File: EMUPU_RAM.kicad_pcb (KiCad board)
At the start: 2 copper layers, 99.1 x 82.5 mm, 29 parts, among them J1 Conn_01x20_Socket, J2 Conn_01x20_Socket, J3 Barrel_Jack_Switch, J4 Conn_01x06_Pin, J5 Conn_01x08_Pin, J6 Conn_01x06_Pin, J7 Conn_01x02_Pin, SW1 SW_SPDT, SW2 SW_SPST, U1 PIC18F57Q43-IPT, U2 HM678127_SOJ32_Arranged

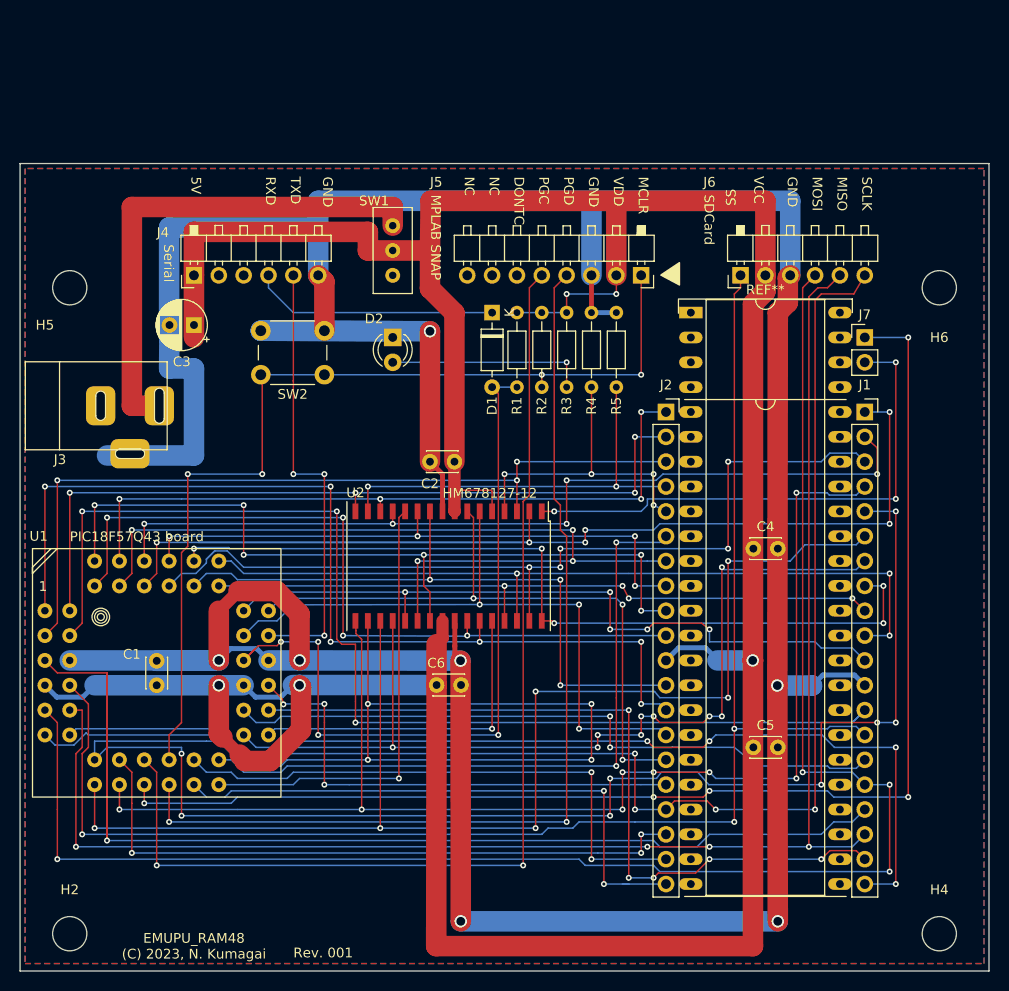
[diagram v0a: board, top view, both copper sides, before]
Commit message: Add Z80 label, RBx jumpers, garbers, ZIP
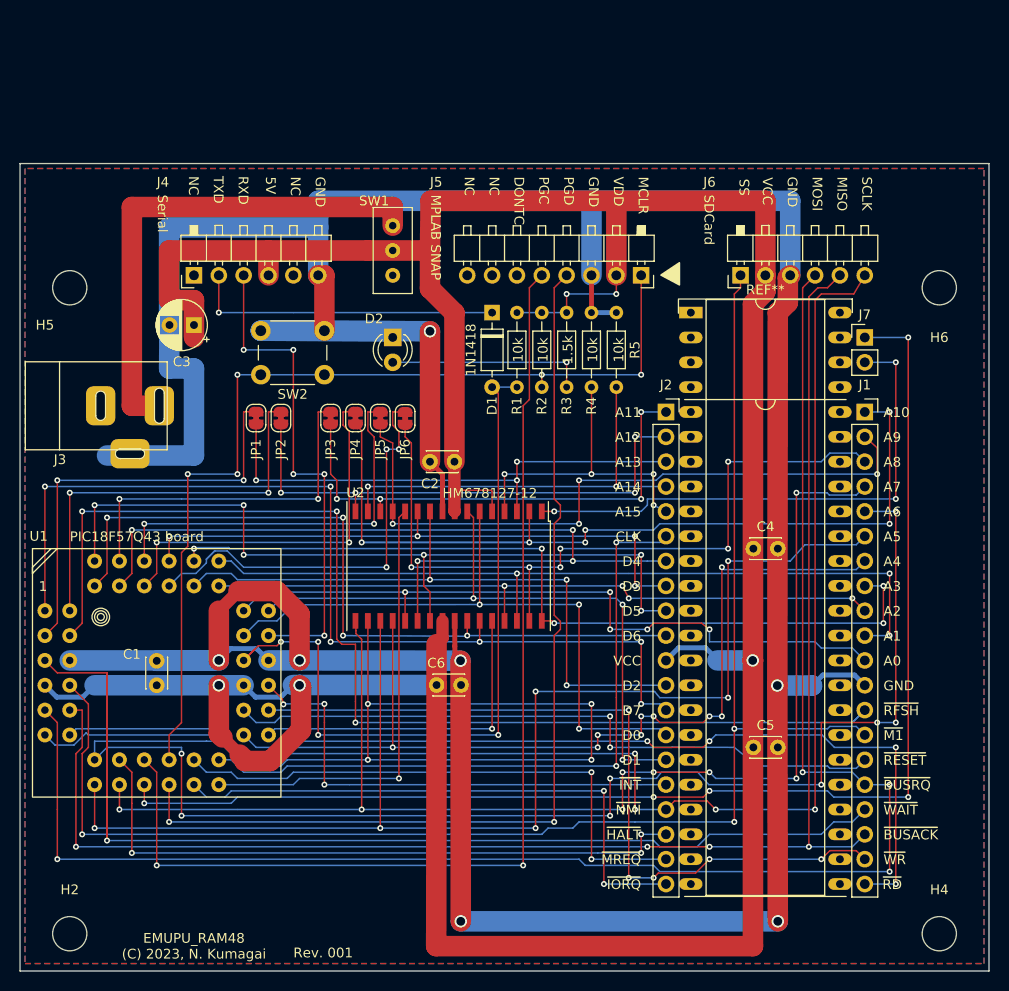
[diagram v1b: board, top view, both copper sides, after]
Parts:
- added JP1: SolderJumper_2_Bridged, Jumper:SolderJumper-2_P1.3mm_Bridged_RoundedPad1.0x1.5mm, F.Cu at (108.0, 84.4)
- added JP2: SolderJumper_2_Bridged, Jumper:SolderJumper-2_P1.3mm_Bridged_RoundedPad1.0x1.5mm, F.Cu at (110.5, 84.4)
- added JP3: SolderJumper_2_Bridged, Jumper:SolderJumper-2_P1.3mm_Bridged_RoundedPad1.0x1.5mm, F.Cu at (115.6, 84.4)
- added JP4: SolderJumper_2_Bridged, Jumper:SolderJumper-2_P1.3mm_Bridged_RoundedPad1.0x1.5mm, F.Cu at (118.1, 84.4)
- added JP5: SolderJumper_2_Bridged, Jumper:SolderJumper-2_P1.3mm_Bridged_RoundedPad1.0x1.5mm, F.Cu at (120.7, 84.4)
- added JP6: SolderJumper_2_Bridged, Jumper:SolderJumper-2_P1.3mm_Bridged_RoundedPad1.0x1.5mm, F.Cu at (123.2, 84.5)
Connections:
- J4 pad 1: VCC -> unconnected-(J4-Pin_1-Pad1)
- J4 pad 2: unconnected-(J4-Pin_2-Pad2) -> Net-(D1-K)
- J4 pad 3: unconnected-(J4-Pin_3-Pad3) -> Net-(J4-Pin_3)
- J4 pad 4: Net-(D1-K) -> VCC
- J4 pad 5: Net-(J4-Pin_5) -> unconnected-(J4-Pin_5-Pad5)
- U1 pad 2: /A12 -> Net-(JP2-B)
- U1 pad 3: /A13 -> Net-(JP1-B)
- U1 pad 33: Net-(J4-Pin_5) -> Net-(J4-Pin_3)
- U1 pad 42: /A8 -> Net-(JP6-B)
- U1 pad 43: /A9 -> Net-(JP5-B)
- U1 pad 44: /A10 -> Net-(JP4-B)
- U1 pad 45: /A11 -> Net-(JP3-B)
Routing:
- net Net-(J4-Pin_3): track 0.00 -> 50.8 mm, vias 0 -> 5
- net Net-(J4-Pin_5): track 45.7 -> 0.00 mm, vias 3 -> 0
- net Net-(JP6-B): track 0.00 -> 44.5 mm, vias 0 -> 3
- net Net-(JP1-B): track 0.00 -> 43.7 mm, vias 0 -> 2
- net Net-(JP2-B): track 0.00 -> 41.9 mm, vias 0 -> 2
- net Net-(JP5-B): track 0.00 -> 40.3 mm, vias 0 -> 2
- net Net-(JP4-B): track 0.00 -> 39.5 mm, vias 0 -> 2
- net Net-(JP3-B): track 0.00 -> 36.8 mm, vias 0 -> 2
- net /A13: track 83.7 -> 52.7 mm
- net /A10: track 132.4 -> 102.1 mm
- net /A12: track 80.6 -> 54.0 mm
- net /A11: track 72.4 -> 51.7 mm
- net /A9: track 89.1 -> 69.5 mm, vias 5 -> 4
- net /A8: track 91.7 -> 78.2 mm, vias 5 -> 6
- net Net-(D1-K): track 25.2 -> 31.8 mm, vias 0 -> 1
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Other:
- board text added: "1.5k"
- board text added: "10k"
- board text added: "A0"
- board text added: "A1"
- board text added: "A10"
- board text added: "A11"
- board text added: "A12"
- board text added: "A13"
- board text added: "A14"
- board text added: "A15"
- board text added: "A2"
- board text added: "A3"
- board text added: "A4"
- board text added: "A5"
- board text added: "A6"
- board text added: "A7"
- board text added: "A8"
- board text added: "A9"
- board text added: "CLK"
- board text added: "D0"
- board text added: "D1"
- board text added: "D2"
- board text added: "D3"
- board text added: "D4"
- board text added: "D5"
- board text added: "D6"
- board text added: "D7"
- board text added: "~{BUSACK}"
- board text added: "~{BUSRQ}"
- board text added: "~{HALT}"
- board text added: "~{INT}"
- board text added: "~{IORQ}"
- board text added: "~{M1}"
- board text added: "~{MREQ}"
- board text added: "~{NMI}"
- board text added: "~{RD}"
- board text added: "~{RESET}"
- board text added: "~{RFSH}"
- board text added: "~{WAIT}"
- board text added: "~{WR}"

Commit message: Ordered version, designated as Rev. 001
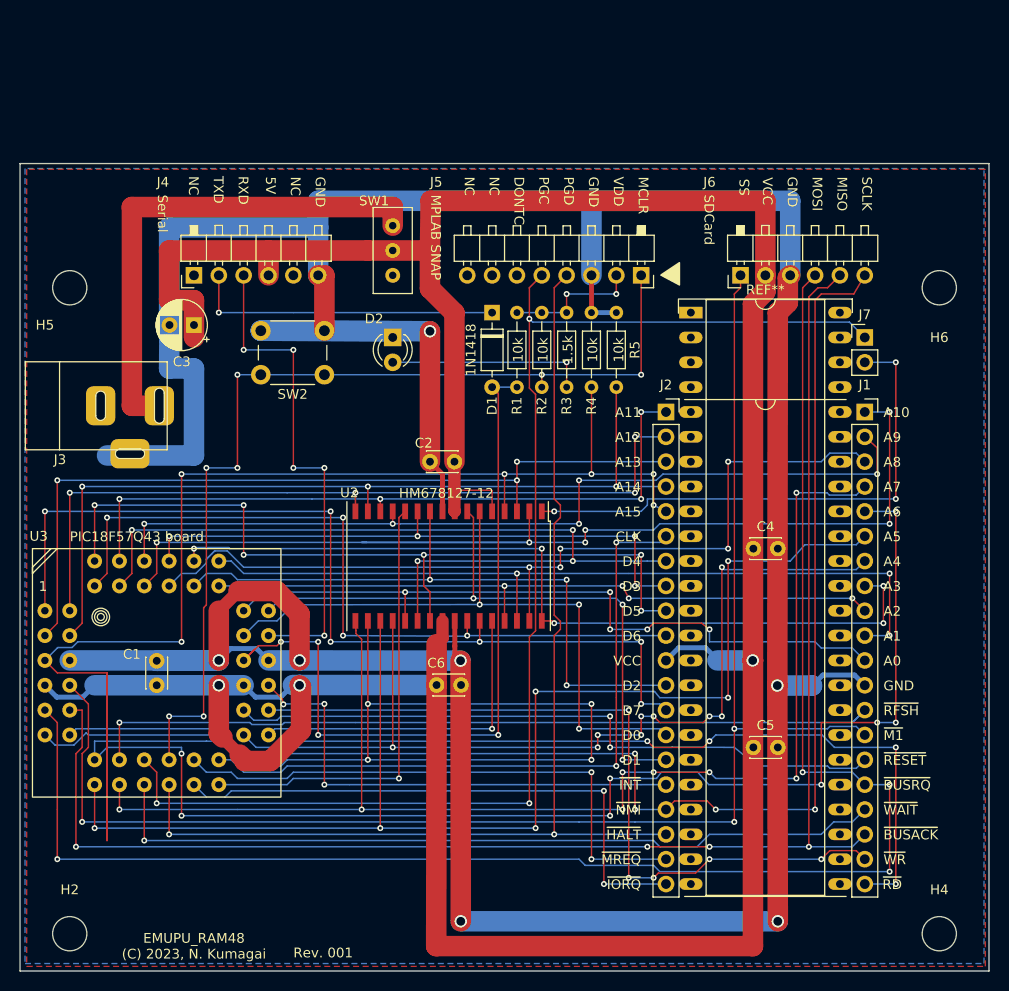
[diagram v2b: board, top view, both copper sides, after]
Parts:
- removed JP1, JP2, JP3, JP4, JP5, JP6: SolderJumper_2_Bridged, Jumper:SolderJumper-2_P1.3mm_Bridged_RoundedPad1.0x1.5mm
- removed U1: PIC18F57Q43-IPT, 0-local:Quad-2x6
- added U3: PIC18F57Q43-IPT, 0-local:Quad-2x6, F.Cu at (86.4, 99.1)
- moved J5 17.9 mm to (129.5, 69.9)
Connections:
- J5 pad 4: Net-(J5-Pin_4) -> /~{HALT}
- J5 pad 5: Net-(J5-Pin_5) -> /RB6
- J7 pad 1: /RB5 -> /RB6
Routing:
- net /RB6: track 0.00 -> 133.2 mm, vias 0 -> 3
- net /RB5: track 132.2 -> 0.00 mm, vias 5 -> 0
- net Net-(J5-Pin_5): track 109.9 -> 0.00 mm, vias 2 -> 0
- net /A15: track 32.5 -> 138.6 mm, vias 4 -> 6
- net Net-(J5-Pin_4): track 100.6 -> 0.00 mm, vias 2 -> 0
- net /~{HALT}: track 66.6 -> 114.6 mm, vias 3 -> 2
- net /A14: track 43.2 -> 88.2 mm, vias 2 -> 3
- net Net-(JP6-B): track 44.5 -> 0.00 mm, vias 3 -> 0
- net Net-(JP1-B): track 43.7 -> 0.00 mm, vias 2 -> 0
- net Net-(JP2-B): track 41.9 -> 0.00 mm, vias 2 -> 0
- net Net-(JP5-B): track 40.3 -> 0.00 mm, vias 2 -> 0
- net Net-(JP4-B): track 39.5 -> 0.00 mm, vias 2 -> 0
- net /~{WAIT}: track 120.5 -> 81.2 mm
- net Net-(JP3-B): track 36.8 -> 0.00 mm, vias 2 -> 0
- net /~{RFSH}: track 116.8 -> 82.4 mm, vias 3 -> 1
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
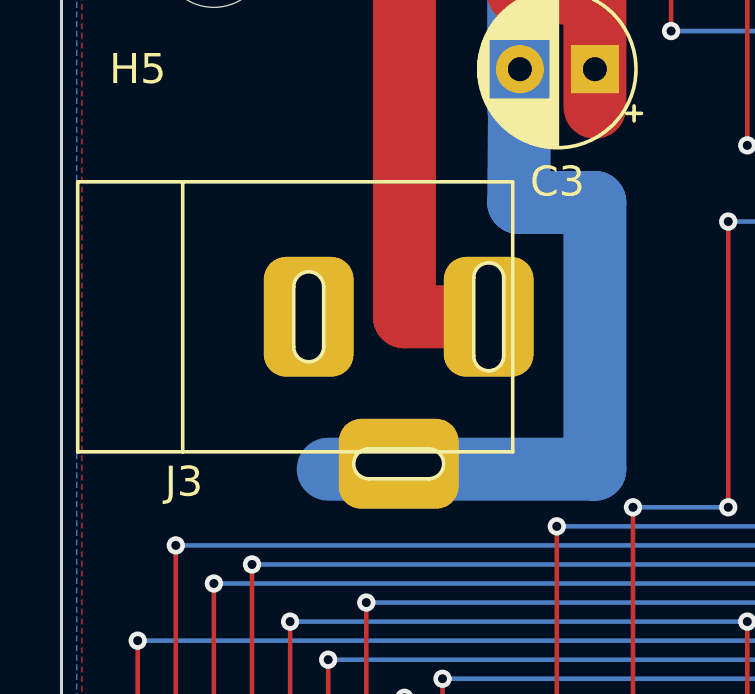
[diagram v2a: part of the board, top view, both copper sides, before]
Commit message: Fix BARREL_JACK footpattern, modify schematic file (Rev002), pcb file fix ongoing
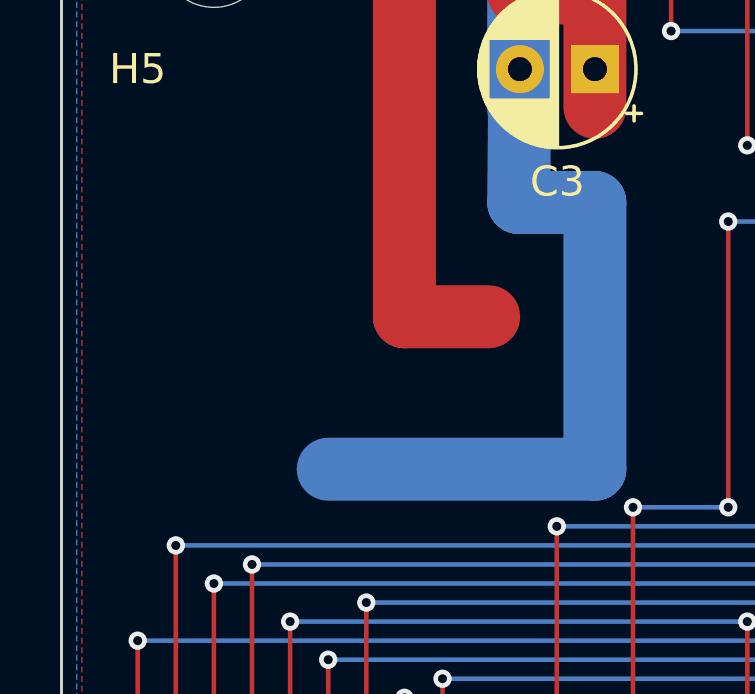
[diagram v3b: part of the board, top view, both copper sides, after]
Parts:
- removed J3: Barrel_Jack_Switch, 0-local:BARREL_JACK

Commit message: New (Rev002) netlist just imported
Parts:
- added J3: Barrel_Jack_Switch, 0-local:BARREL_JACK, F.Cu at (93.1, 48.3)
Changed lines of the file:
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@@
   (net 55 "Net-(U2-~{OE})")
   (net 56 "/RB6")
+  (net 57 "unconnected-(J3-Pad3)")
   (footprint "LED_THT:LED_D3.0mm" (layer "F.Cu")
     (at 121.92 76.2 -90)
@@
     )
   )
+  (footprint "0-local:BARREL_JACK" (layer "F.Cu")
+    (at 93.075 48.261)
+    (descr "MJ179PH - Akizuki's DC Jack")
+    (tags "DC Jack Barrel_Jack")
+    (property "Sheetfile" "EMUPU_RAM.kicad_sch")
+    (property "Sheetname" "")
+    (property "ki_description" "DC Barrel Jack with an internal switch")
+    (property "ki_keywords" "DC power barrel jack connector")
+    (attr through_hole)
+    (fp_text reference "J3" (at -6.915 5.499) (layer "F.SilkS")
+        (effects (font (size 1 1) (thickness 0.15)))
+    )
+    (fp_text value "Barrel_Jack_Switch" (at -0.015 -5.715) (layer "F.Fab")
+        (effects (font (size 1 1) (thickness 0.15)))
+    )
+    (fp_line (start -7.715 -4.501) (end -7.715 4.499)
+      (stroke (width 0.12) (type solid)) (layer "F.SilkS"))
+    (fp_line (start -7.715 4.499) (end 6.785 4.499)
+      (stroke (width 0.12) (type solid)) (layer "F.SilkS"))
+    (fp_line (start -4.215 4.499) (end -4.215 -4.501)
+      (stroke (width 0.12) (type solid)) (layer "F.SilkS"))
+    (fp_line (start -0.515 0.999) (end -0.515 -1.001)
+      (stroke (width 0.12) (type solid)) (layer "F.SilkS"))
+    (fp_line (start 0.485 -1.001) (end 0.485 0.999)
+      (stroke (width 0.12) (type solid)) (layer "F.SilkS"))
+    (fp_line (start 1.985 4.399) (end 3.985 4.399)
+      (stroke (width 0.12) (type solid)) (layer "F.SilkS"))
+    (fp_line (start 1.985 5.399) (end 3.985 5.399)
+      (stroke (width 0.12) (type solid)) (layer "F.SilkS"))
+    (fp_line (start 5.485 1.299) (end 5.485 -1.301)
+      (stroke (width 0.12) (type solid)) (layer "F.SilkS"))
+    (fp_line (start 6.485 -1.301) (end 6.485 1.299)
+      (stroke (width 0.12) (type solid)) (layer "F.SilkS"))
+    (fp_line (start 6.785 -4.501) (end -7.715 -4.501)
+      (stroke (width 0.12) (type solid)) (layer "F.SilkS"))
+    (fp_line (start 6.785 4.499) (end 6.785 -4.501)
+      (stroke (width 0.12) (type solid)) (layer "F.SilkS"))
+    (fp_arc (start -0.515 -1.001) (mid -0.015 -1.501) (end 0.485 -1.001)
+      (stroke (width 0.12) (type solid)) (layer "F.SilkS"))
+    (fp_arc (start 0.485 0.999) (mid -0.015 1.499) (end -0.515 0.999)
+      (stroke (width 0.12) (type solid)) (layer "F.SilkS"))
+    (fp_arc (start 1.985 5.399) (mid 1.485 4.899) (end 1.985 4.399)
+      (stroke (width 0.12) (type solid)) (layer "F.SilkS"))
+    (fp_arc (start 3.985 4.399) (mid 4.485 4.899) (end 3.985 5.399)
+      (stroke (width 0.12) (type solid)) (layer "F.SilkS"))
+    (fp_arc (start 5.485 -1.301) (mid 5.985 -1.801) (end 6.485 -1.301)
+      (stroke (width 0.12) (type solid)) (layer "F.SilkS"))
+    (fp_arc (start 6.485 1.299) (mid 5.985 1.799) (end 5.485 1.299)
+      (stroke (width 0.12) (type solid)) (layer "F.SilkS"))
+    (fp_line (start -7.815 -4.701) (end 6.985 -4.701)
+      (stroke (width 0.12) (type solid)) (layer "F.CrtYd"))
+    (fp_line (start -7.815 4.699) (end -7.815 -4.701)
+      (stroke (width 0.12) (type solid)) (layer "F.CrtYd"))
+    (fp_line (start 0.885 4.699) (end -7.815 4.699)
+      (stroke (width 0.12) (type solid)) (layer "F.CrtYd"))
+    (fp_line (start 0.885 6.499) (end 0.885 4.699)
+      (stroke (width 0.12) (type solid)) (layer "F.CrtYd"))
+    (fp_line (start 5.085 4.699) (end 5.085 5.599)
+      (stroke (width 0.12) (type solid)) (layer "F.CrtYd"))
+    (fp_line (start 5.085 5.599) (end 5.085 6.099)
+      (stroke (width 0.12) (type solid)) (layer "F.CrtYd"))
+    (fp_line (start 5.085 6.099) (end 5.085 6.499)
+      (stroke (width 0.12) (type solid)) (layer "F.CrtYd"))
+    (fp_line (start 5.085 6.499) (end 0.885 6.499)
+      (stroke (width 0.12) (type solid)) (layer "F.CrtYd"))
+    (fp_line (start 6.985 -4.701) (end 6.985 -2.101)
+      (stroke (width 0.12) (type solid)) (layer "F.CrtYd"))
+    (fp_line (start 6.985 -2.101) (end 7.185 -2.101)
+      (stroke (width 0.12) (type solid)) (layer "F.CrtYd"))
+    (fp_line (start 6.985 2.099) (end 6.985 4.699)
+      (stroke (width 0.12) (type solid)) (layer "F.CrtYd"))
+    (fp_line (start 6.985 4.699) (end 5.085 4.699)
+      (stroke (width 0.12) (type solid)) (layer "F.CrtYd"))
+    (fp_line (start 7.185 -2.101) (end 7.485 -1.901)
+      (stroke (width 0.12) (type solid)) (layer "F.CrtYd"))
+    (fp_line (start 7.185 2.099) (end 6.985 2.099)
+      (stroke (width 0.12) (type solid)) (layer "F.CrtYd"))
+    (fp_line (start 7.485 -1.901) (end 7.685 -1.501)
+      (stroke (width 0.12) (type solid)) (layer "F.CrtYd"))
+    (fp_line (start 7.485 1.899) (end 7.185 2.099)
+      (stroke (width 0.12) (type solid)) (layer "F.CrtYd"))
+    (fp_line (start 7.685 -1.501) (end 7.685 1.699)
+      (stroke (width 0.12) (type solid)) (layer "F.CrtYd"))
+    (fp_line (start 7.685 1.699) (end 7.485 1.899)
+      (stroke (width 0.12) (type solid)) (layer "F.CrtYd"))
+    (pad "1" thru_hole roundrect (at 5.985 -0.001) (size 3 4) (drill oval 1 3.5) (layers "*.Cu" "*.Mask") (roundrect_rratio 0.25)
+      (net 53 "Net-(SW1-C)") (pintype "passive"))
+    (pad "2" thru_hole roundrect (at -0.015 -0.001) (size 3 4) (drill oval 1 3) (layers "*.Cu" "*.Mask") (roundrect_rratio 0.25)
+      (net 11 "GND") (pintype "passive"))
+    (pad "3" thru_hole roundrect (at 2.985 4.899) (size 4 3) (drill oval 3 1) (layers "*.Cu" "*.Mask") (roundrect_rratio 0.25)
+      (net 57 "unconnected-(J3-Pad3)") (pintype "passive+no_connect"))
+  )
   (footprint "Connector_PinSocket_2.54mm:PinSocket_1x20_P2.54mm_Vertical" (layer "F.Cu")
     (at 170.18 83.82)
@@
     (connect_pads (clearance 0.35))
     (min_thickness 0.254) (filled_areas_thickness no)
-    (fill yes (thermal_gap 0.5) (thermal_bridge_width 0.508))
+    (fill (thermal_gap 0.5) (thermal_bridge_width 0.508))
     (polygon
       (pts
@@
     (connect_pads (clearance 0.35))
     (min_thickness 0.25) (filled_areas_thickness no)
-    (fill yes (thermal_gap 0.5) (thermal_bridge_width 0.5))
+    (fill (thermal_gap 0.5) (thermal_bridge_width 0.5))
     (polygon
       (pts

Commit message: EMUPU_RAM48_Rev002. pcb modifying completed
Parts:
- added R6: 10k, Resistor_THT:R_Axial_DIN0204_L3.6mm_D1.6mm_P7.62mm_Horizontal, F.Cu at (111.8, 132.1)
- moved J3 35.1 mm to (92.3, 83.4)
- moved R5 7.62 mm to (144.8, 73.7), turned to -90 degrees
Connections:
- net /RB6 renamed /TEST
- J4 pad 2: Net-(D1-K) -> Net-(J4-Pin_2)
- J4 pad 3: Net-(J4-Pin_3) -> Net-(D1-K)
- J5 pad 4: /~{HALT} -> /~{WAIT}
- J6 pad 1: /~{M1} -> Net-(J6-Pin_1)
- J6 pad 4: /~{BUSRQ} -> Net-(J6-Pin_4)
- J6 pad 5: /~{BUSAK} -> Net-(J6-Pin_5)
- J6 pad 6: /~{NMI} -> Net-(J6-Pin_6)
- R4 pad 1: /A15 -> /A16
- R5 pad 1: /A14 -> VCC
- R5 pad 2: GND -> Net-(U2-~{OE})
- U2 pad 5: VCC -> GND
- U3 pad 10: /~{BUSAK} -> Net-(J6-Pin_5)
- U3 pad 11: /~{NMI} -> Net-(J6-Pin_6)
- U3 pad 17: /~{WAIT} -> /~{M1}
- U3 pad 19: /~{HALT} -> /~{WAIT}
- U3 pad 27: /~{WR} -> /~{BUSRQ}
- U3 pad 33: Net-(J4-Pin_3) -> Net-(J4-Pin_2)
- U3 pad 8: /~{M1} -> Net-(J6-Pin_1)
- U3 pad 9: /~{BUSRQ} -> Net-(J6-Pin_4)
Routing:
- net /~{BUSAK}: track 157.0 -> 0.00 mm, vias 4 -> 0
- net Net-(J6-Pin_4): track 0.00 -> 154.0 mm, vias 0 -> 2
- net Net-(J6-Pin_5): track 0.00 -> 150.7 mm, vias 0 -> 4
- net /~{NMI}: track 146.0 -> 0.00 mm, vias 4 -> 0
- net Net-(J6-Pin_6): track 0.00 -> 142.8 mm, vias 0 -> 3
- net Net-(J6-Pin_1): track 0.00 -> 137.8 mm, vias 0 -> 2
- net /~{HALT}: track 114.6 -> 0.00 mm, vias 2 -> 0
- net /~{BUSRQ}: track 171.0 -> 90.9 mm, vias 4 -> 6
- net /~{WR}: track 79.6 -> 0.00 mm, vias 5 -> 0
- net /~{WAIT}: track 81.2 -> 136.4 mm, vias 1 -> 4
- net Net-(J4-Pin_2): track 0.00 -> 53.3 mm, vias 0 -> 5
- net /~{M1}: track 151.6 -> 98.4 mm
- net Net-(J4-Pin_3): track 50.8 -> 0.00 mm, vias 5 -> 0
- net Net-(U2-~{OE}): track 34.1 -> 72.8 mm, vias 1 -> 3
- net /A16: track 54.3 -> 67.0 mm, vias 3 -> 4
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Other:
- board text added: "1"
- board text added: "Rev. 002"
- board text removed: "Rev. 001"
